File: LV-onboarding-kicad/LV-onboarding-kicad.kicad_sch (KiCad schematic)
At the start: 20 parts, among them J1 Current Transducer HASS 50-S, J2 AiM Sports Pressure Sensors X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, K1 Relay_SPST-NO, U1 NE555D, U1a ${SIM.PARAMS}, U1b ${SIM.PARAMS}, U1c ${SIM.PARAMS}, U2 ${SIM.PARAMS}, U4 74AHC1G08

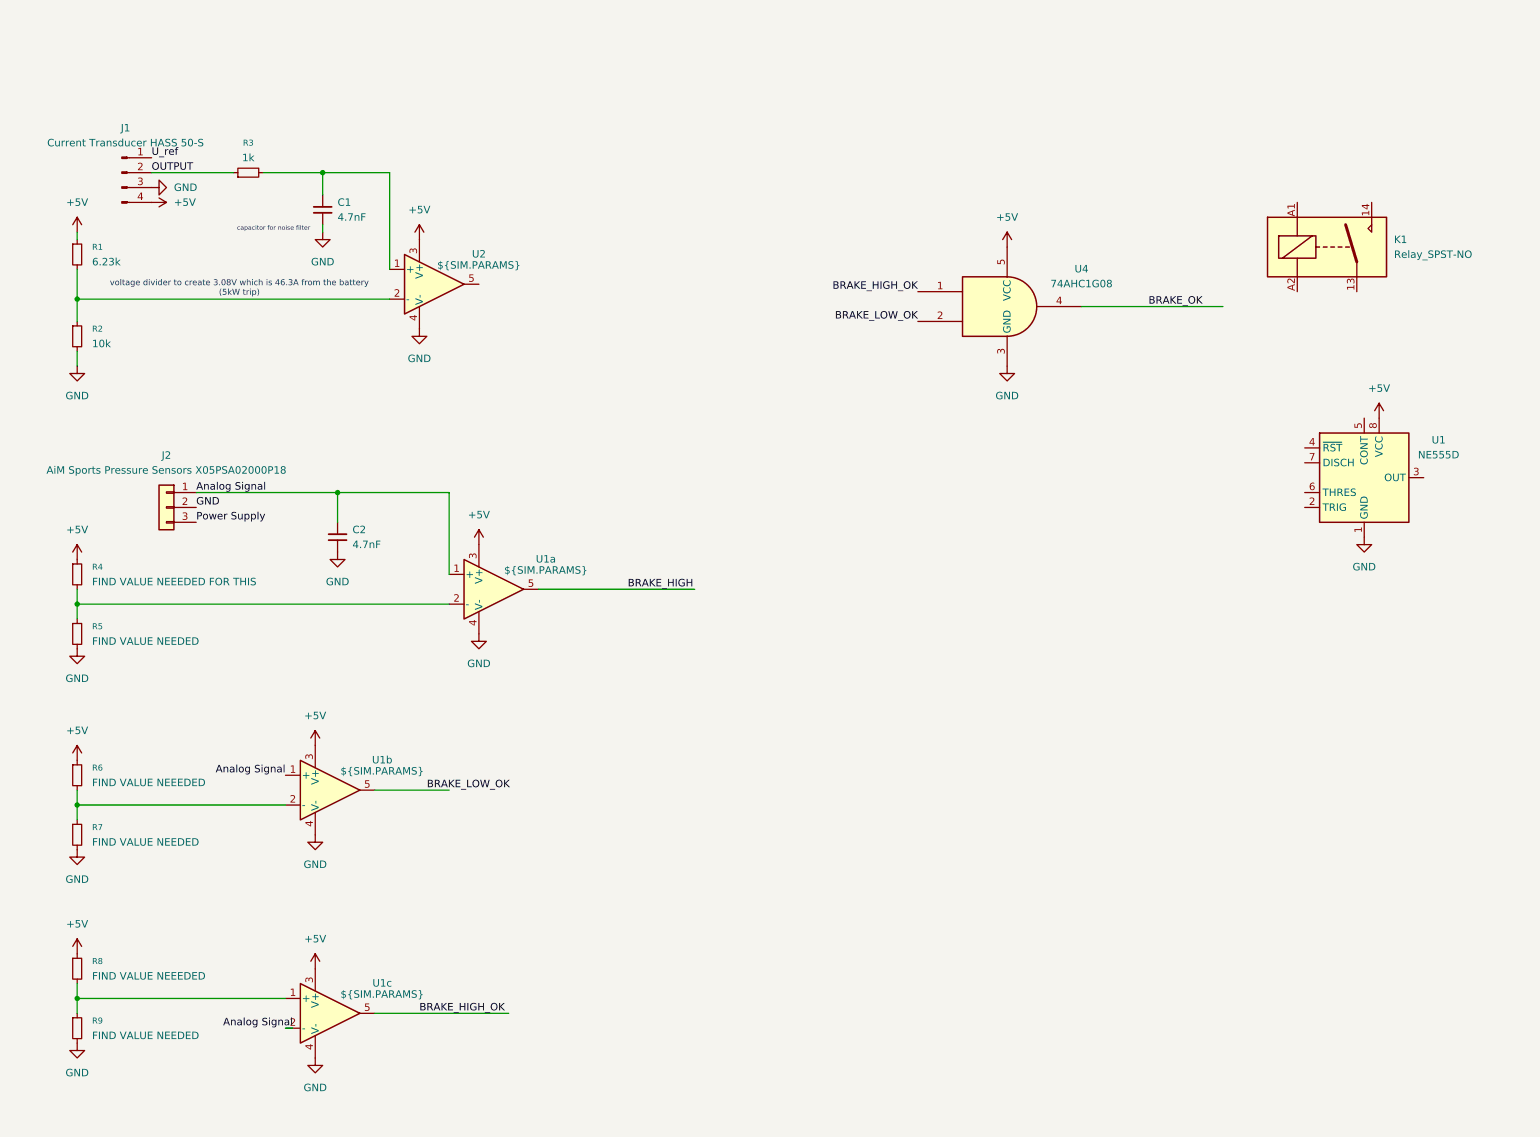
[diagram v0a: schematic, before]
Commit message: BSPD sensors
finished making the logic gate setup for the comparators checking for short/open circuit
made more sheets for other sections
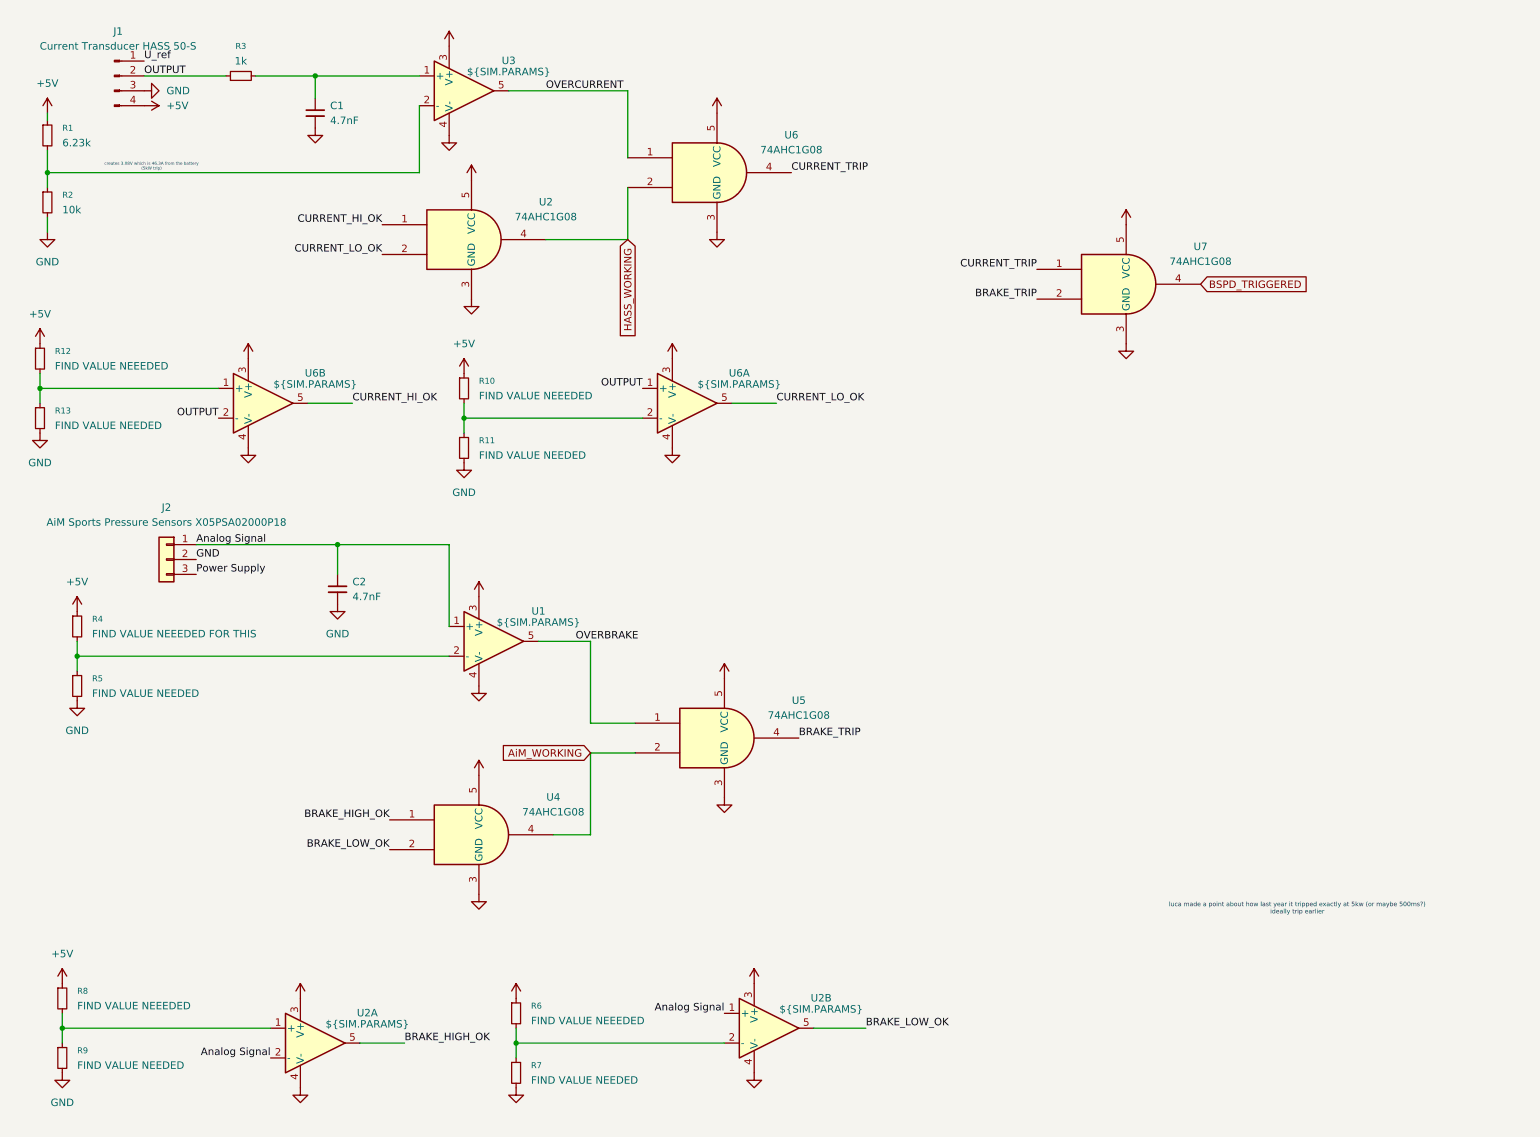
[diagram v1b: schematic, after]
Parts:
- removed K1: Relay_SPST-NO, Relay_THT:Relay_NCR_HHG1D-1, symbol Relay:Relay_SPST-NO
- removed U1: NE555D, Package_SO:SOIC-8_3.9x4.9mm_P1.27mm, symbol Timer:NE555D
- added R10, R12: FIND VALUE NEEEDED, symbol Device:R_Small
- added R11, R13: FIND VALUE NEEDED, symbol Device:R_Small
- added U2, U6, U7: 74AHC1G08, symbol 74xGxx:74AHC1G08
- added U5: 74AHC1G08, Package_SON:USON-20_2x4mm_P0.4mm, symbol 74xGxx:74AHC1G08
- added U6A, U6B: ${SIM.PARAMS}, Package_SO:SSOP-24_3.9x8.7mm_P0.635mm, symbol Simulation_SPICE:OPAMP
- renumbered U1a to U1, U1c to U2A, U1b to U2B, U2 to U3
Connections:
- net +5V: now also R10.1, R12.1, U2.5 (VCC), U5.5 (VCC), U6.5 (VCC), U6A.3 (V+), U6B.3 (V+), U7.5 (VCC)
- net GND: now also R11.2, R13.2, U2.3 (GND), U5.3 (GND), U6.3 (GND), U6A.4 (V-), U6B.4 (V-), U7.3 (GND)
- net OUTPUT: now also U6A.1 (+), U6B.2 (-)
- net OVERCURRENT: now reaches U3.5
- net OVERCURRENT: now also U6.1
- net BRAKE_HIGH renamed OVERBRAKE
- net OVERBRAKE: now also U5.1
- net BRAKE_OK renamed AiM_WORKING
- net AiM_WORKING: now also U5.2
- new net: R10.2, R11.1, U6A.2 (-)
- new net: R12.2, R13.1, U6B.1 (+)
- new net BRAKE_TRIP: U5.4, U7.2
- new net BSPD_TRIGGERED: U7.4
- new net CURRENT_HI_OK: U2.1, U6B.5
- new net CURRENT_LO_OK: U2.2, U6A.5
- new net CURRENT_TRIP: U6.4, U7.1
- new net HASS_WORKING: U2.4, U6.2
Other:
- note added: "luca made a point about how last year it tripped exactly at 5kw (or maybe 500ms?) ideally trip earlier"
- note removed: "capacitor for noise filter"
- note removed: "voltage divider to create 3.08V which is 46.3A from the battery (5kW trip)"
- moved on the sheet: C1, C2, J1, J2, R1, R2, R3, R4, R5, R6, R7, R8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

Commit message: op amp study
needed a refresher on op amps so I did some LTSpice
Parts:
- removed J1: Current Transducer HASS 50-S, Package_DFN_QFN:QFN-20-1EP_5x5mm_P0.65mm_EP3.35x3.35mm, symbol Connector:Conn_01x04_Pin
- added J3: Conn_01x04, Package_DFN_QFN:QFN-20-1EP_5x5mm_P0.65mm_EP3.35x3.35mm, symbol Connector_Generic:Conn_01x04
- added U10, U8: SN74LVC1G00DCK, Package_TO_SOT_SMD:Texas_R-PDSO-G5_DCK-5, symbol 74xGxx:SN74LVC1G00DCK
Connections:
- net +5V: now also J3.4 (Pin_4)
- net GND: now also J3.3 (Pin_3)
- net OUTPUT: now also J3.2 (Pin_2)
- new net U_Ref: J3.1 (Pin_1)
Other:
- note added: "inverting op amp"
- note added: "non inverting op amp"
- note added: "when a fault happens, current_lo/hi_ok is at high"

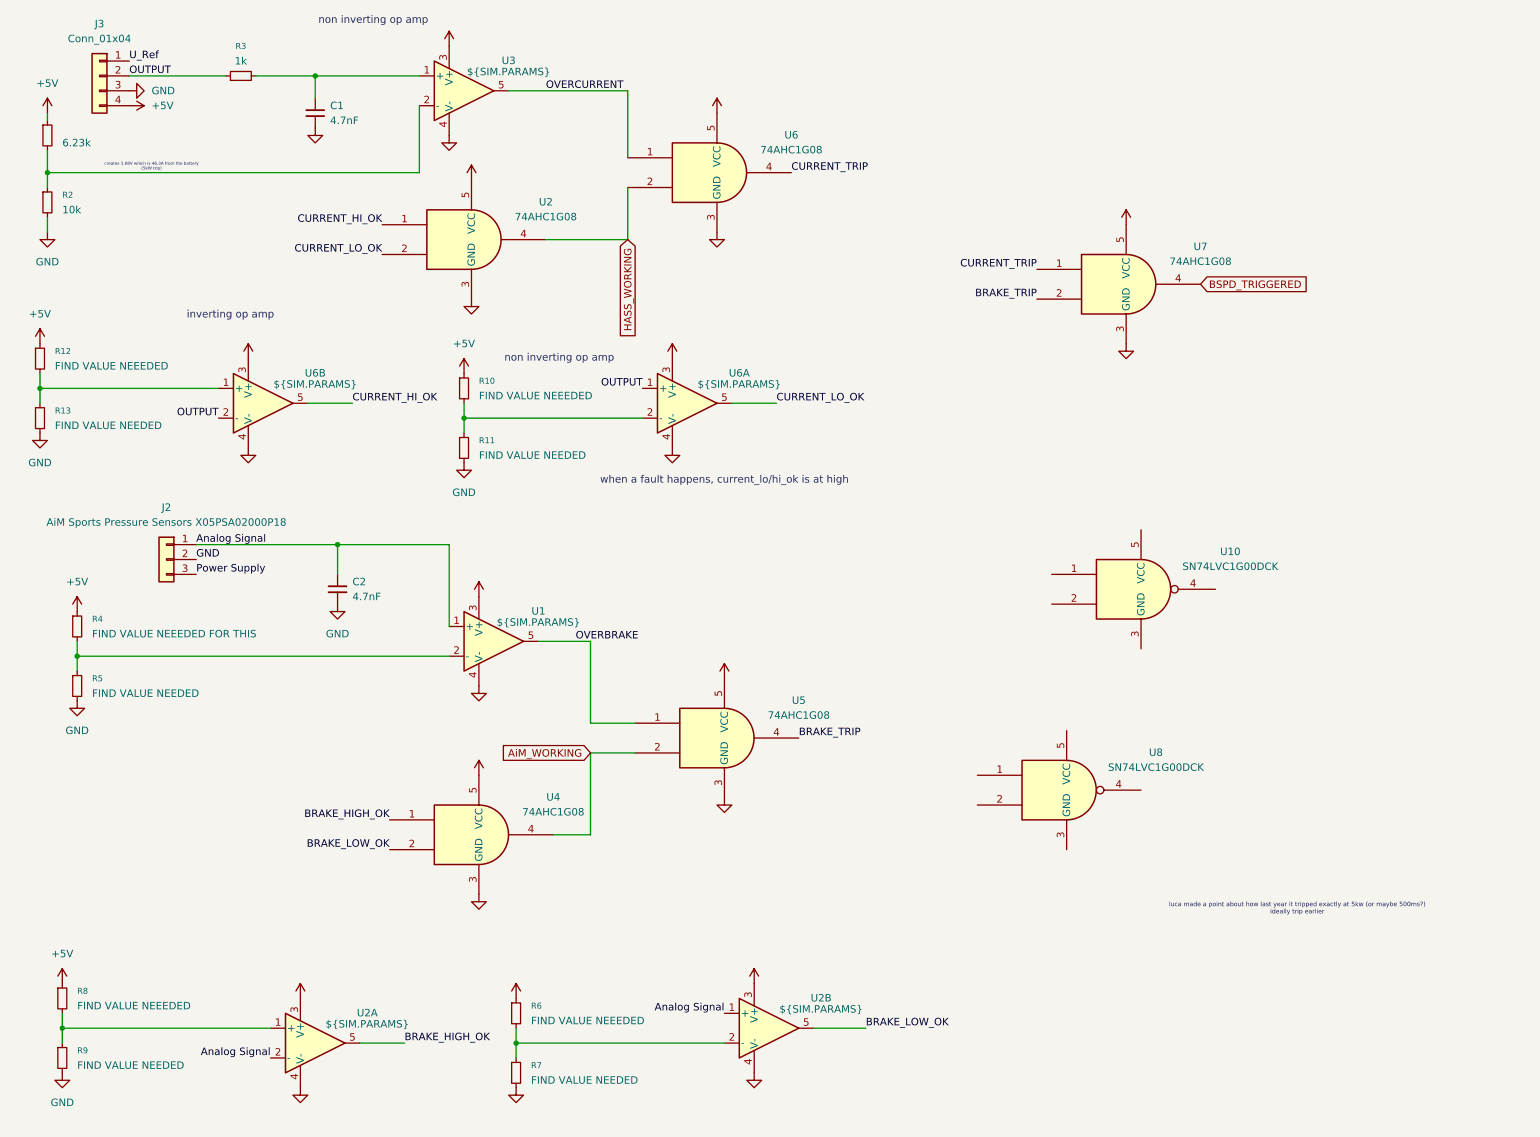
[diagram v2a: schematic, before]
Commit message: worked in BSPD
checked the datasheet for HASS sensor and made a low pass filter in LTSpice
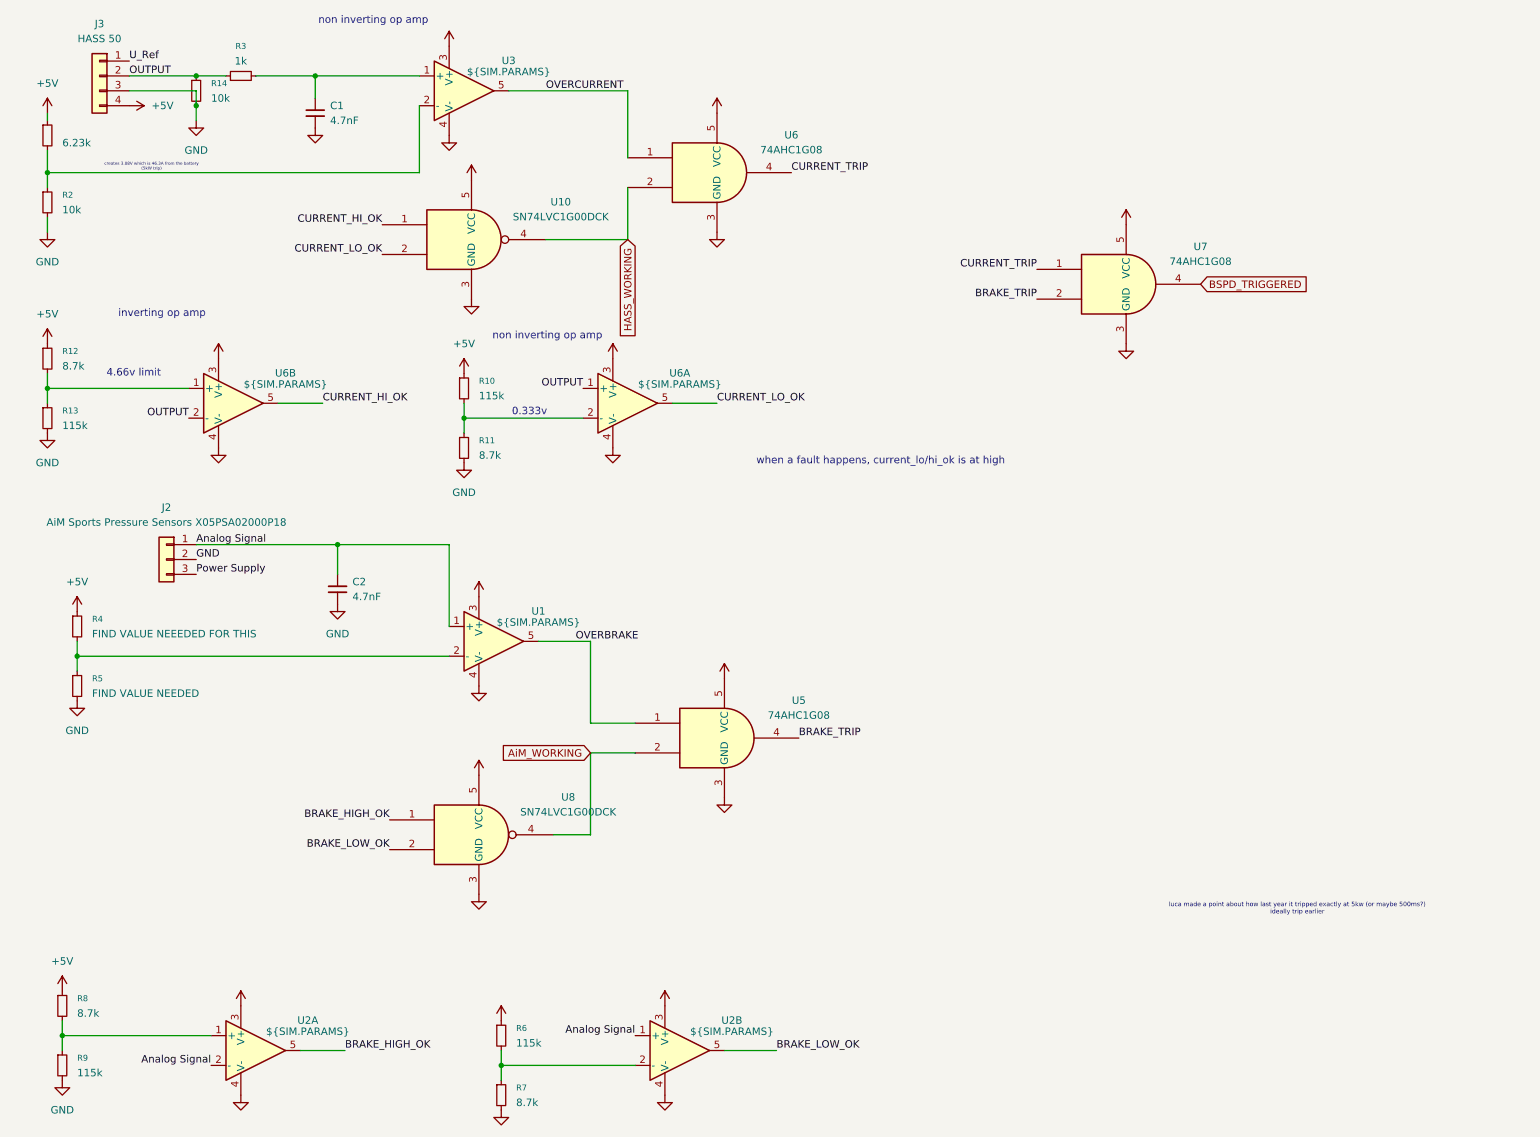
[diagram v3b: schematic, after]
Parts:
- removed U2: 74AHC1G08, symbol 74xGxx:74AHC1G08
- removed U4: 74AHC1G08, Package_SON:USON-20_2x4mm_P0.4mm, symbol 74xGxx:74AHC1G08
- added R14: 10k, Package_TO_SOT_SMD:Texas_R-PDSO-G5_DCK-5, symbol Device:R_Small
- J3: value Conn_01x04 -> HASS 50
- R10, R6: value FIND VALUE NEEEDED -> 115k
- R11, R7: value FIND VALUE NEEDED -> 8.7k
- R12, R8: value FIND VALUE NEEEDED -> 8.7k
- R13, R9: value FIND VALUE NEEDED -> 115k
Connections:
- net +5V: now also U10.5 (VCC), U8.5 (VCC)
- net AiM_WORKING: now also U8.4
- net BRAKE_HIGH_OK: now also U8.1
- net BRAKE_LOW_OK: now also U8.2
- net CURRENT_HI_OK: now also U10.1
- net CURRENT_LO_OK: now also U10.2
- net GND: now also U10.3 (GND), U8.3 (GND), R14.2
- net HASS_WORKING: now also U10.4
- net OUTPUT: now also R14.1
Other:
- note added: "0.333v"
- note added: "4.66v limit"
- moved on the sheet: R12, R13, R6, R7, R8, R9, U10, U2A, U2B, U6A, U6B, U8

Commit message: fixed logic in BSPD
changed NAND gates to NOT and AND gates
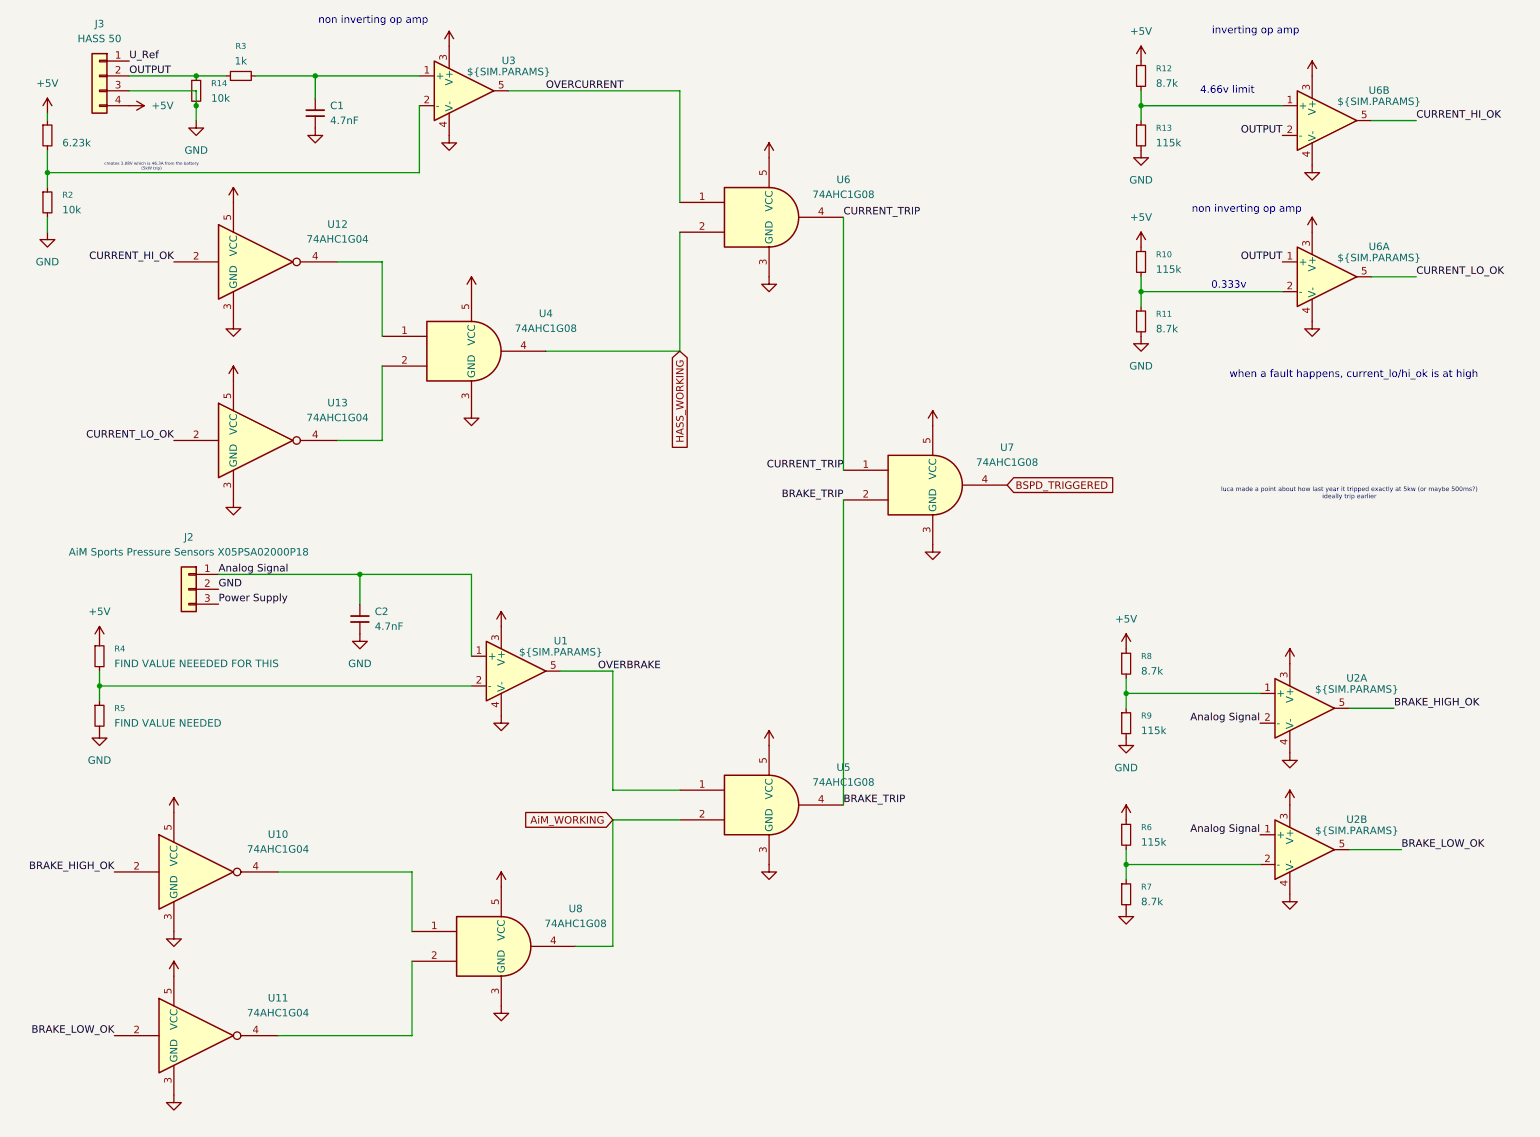
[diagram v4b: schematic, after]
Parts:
- removed U10, U8: SN74LVC1G00DCK, Package_TO_SOT_SMD:Texas_R-PDSO-G5_DCK-5, symbol 74xGxx:SN74LVC1G00DCK
- added U10, U11, U12, U13: 74AHC1G04, symbol 74xGxx:74AHC1G04
- added U4, U8: 74AHC1G08, symbol 74xGxx:74AHC1G08
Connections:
- net +5V: now also U10.5 (VCC), U11.5 (VCC), U12.5 (VCC), U13.5 (VCC), U4.5 (VCC), U8.5 (VCC)
- net AiM_WORKING: now also U8.4
- net BRAKE_HIGH_OK: now also U10.2
- net BRAKE_LOW_OK: now also U11.2
- net CURRENT_HI_OK: now also U12.2
- net CURRENT_LO_OK: now also U13.2
- net GND: now also U10.3 (GND), U11.3 (GND), U12.3 (GND), U13.3 (GND), U4.3 (GND), U8.3 (GND)
- net HASS_WORKING: now also U4.4
- new net: U11.4, U8.2
- new net: U13.4, U4.2
- new net: U10.4, U8.1
- new net: U12.4, U4.1
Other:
- moved on the sheet: C2, J2, R10, R11, R12, R13, R4, R5, R6, R7, R8, R9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
